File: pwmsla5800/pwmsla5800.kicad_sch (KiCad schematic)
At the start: 26 parts, among them Q1 BC547, Q2 BC547, U1 LM324

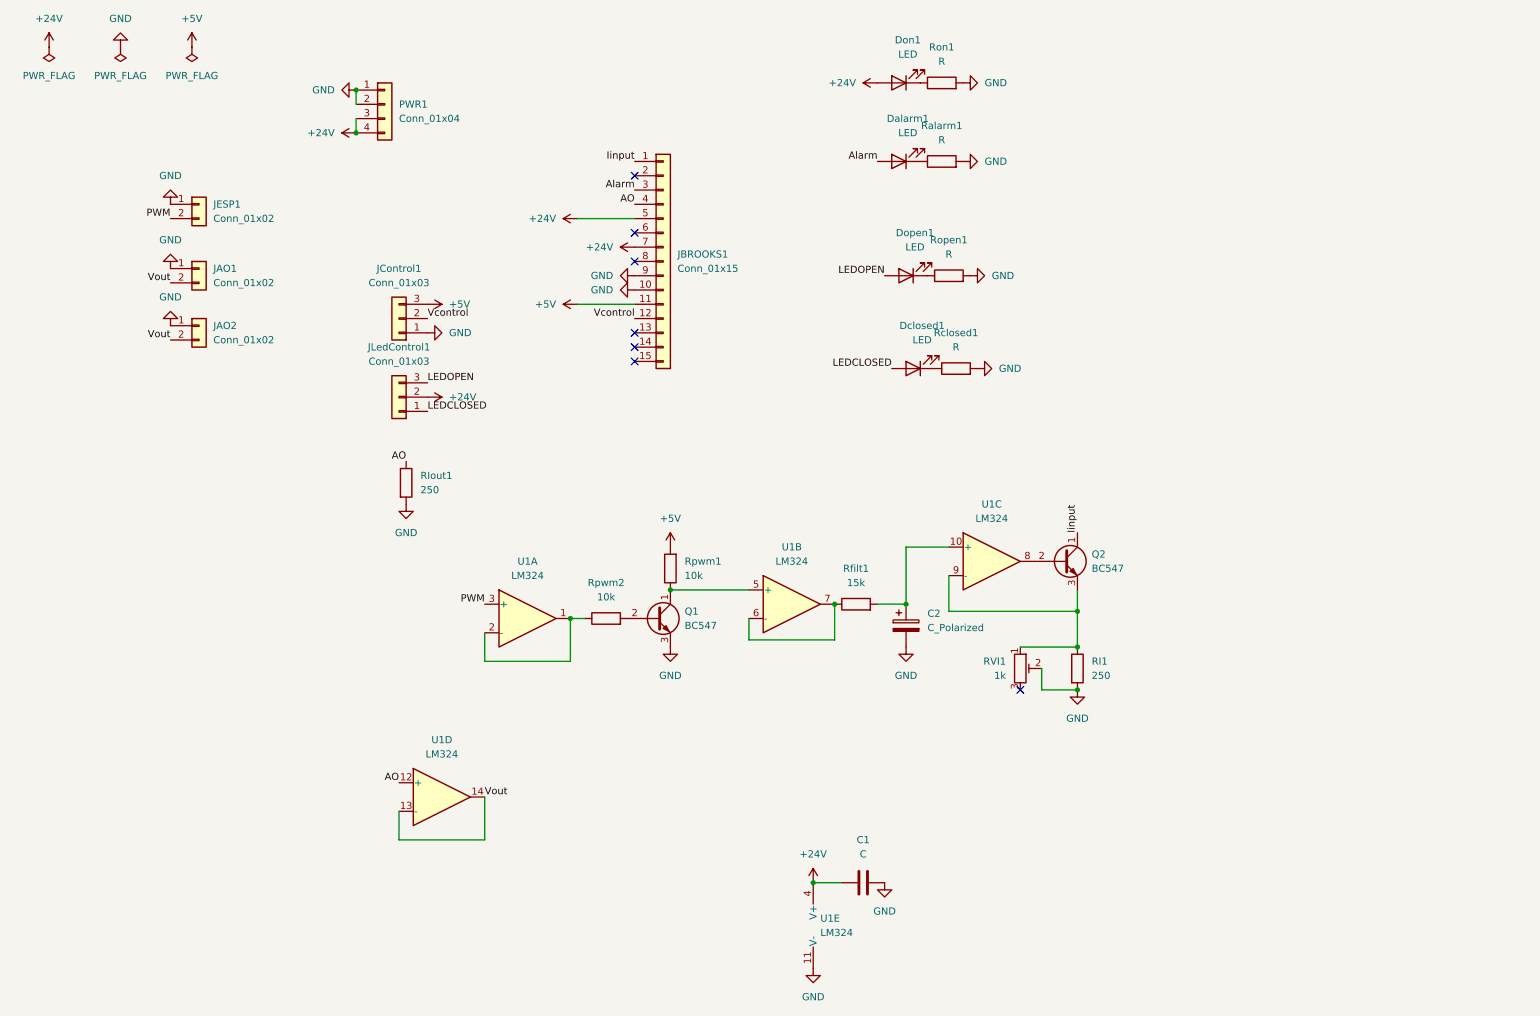
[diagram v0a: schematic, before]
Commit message: New concept. Generating the 4-20mA current is done on an outside module
Until I figure out how generate the current well, I think it is better just use a Chinese board.

When generating the PWM, to obtain a stable voltage I am using a TL431 circuit.
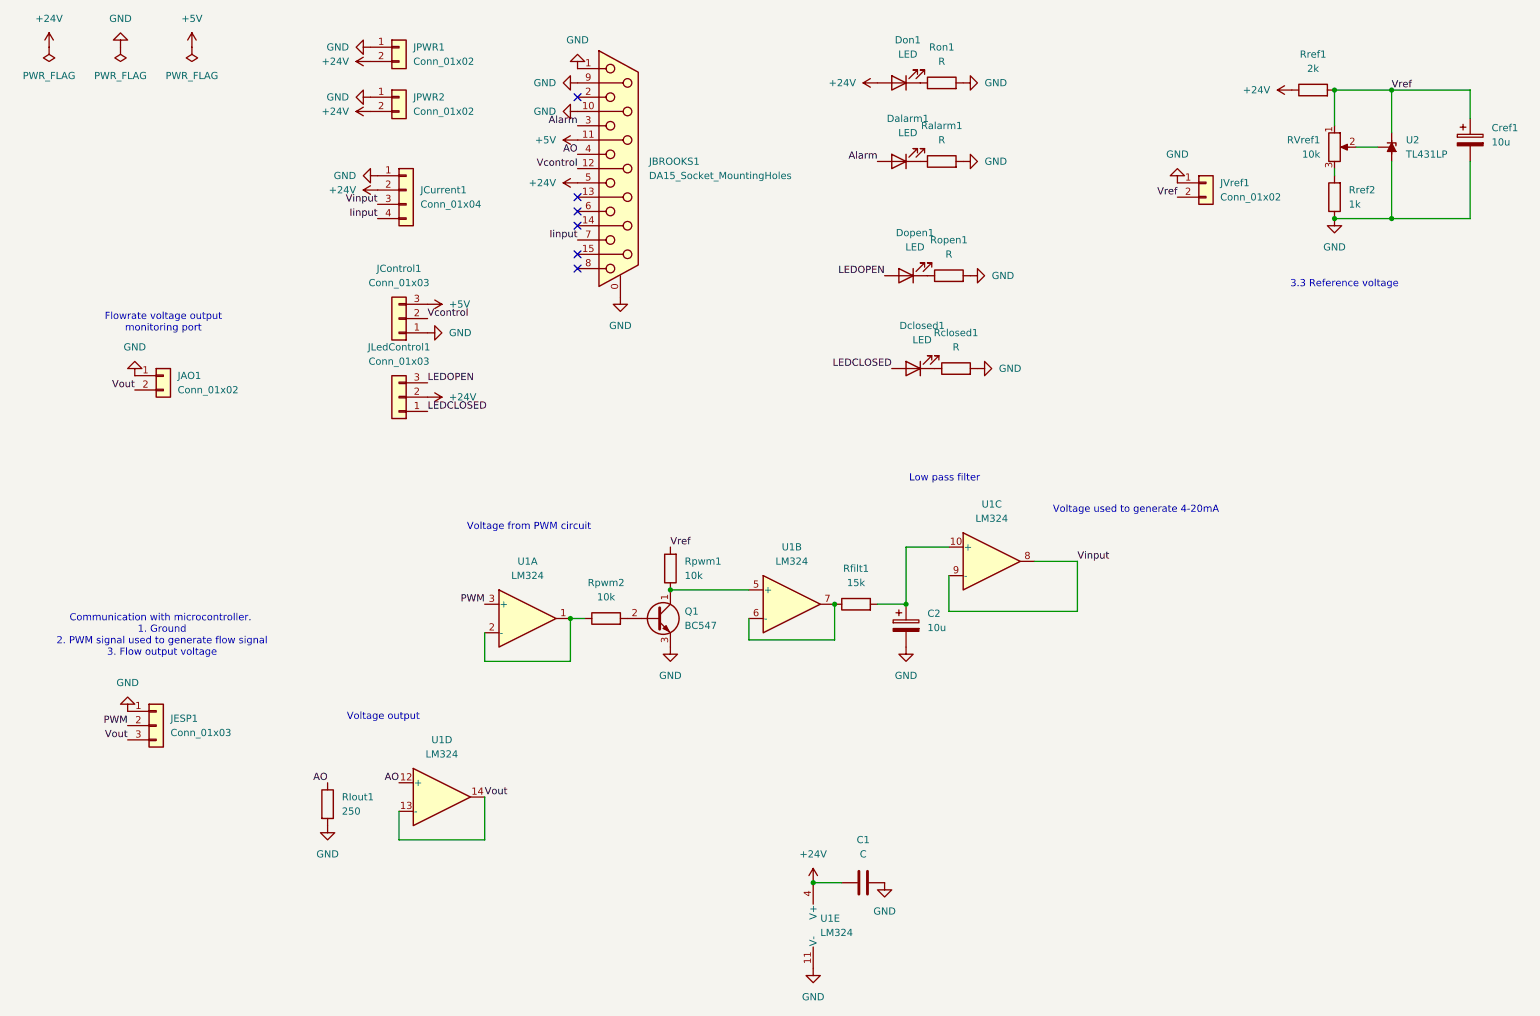
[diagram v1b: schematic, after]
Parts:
- removed JAO2, JESP1: Conn_01x02, Connector_PinHeader_2.54mm:PinHeader_1x02_P2.54mm_Vertical, symbol Connector_Generic:Conn_01x02
- removed JBROOKS1: Conn_01x15, Connector_Dsub:DSUB-15_Socket_Horizontal_P2.77x2.84mm_EdgePinOffset4.94mm_Housed_MountingHolesOffset4.94mm, symbol Connector_Generic:Conn_01x15
- removed PWR1: Conn_01x04, TerminalBlock:TerminalBlock_bornier-4_P5.08mm, symbol Connector_Generic:Conn_01x04
- removed Q2: BC547, Package_TO_SOT_THT:TO-92_Inline_Wide, symbol Transistor_BJT:BC547
- removed RI1: 250, Resistor_THT:R_Axial_DIN0207_L6.3mm_D2.5mm_P10.16mm_Horizontal, symbol Device:R
- removed RVI1: 1k, Potentiometer_THT:Potentiometer_Bourns_3296W_Vertical, symbol Device:R_Potentiometer_Trim
- added Cref1: 10u, Capacitor_THT:CP_Radial_D6.3mm_P2.50mm, symbol Device:C_Polarized
- added JBROOKS1: DA15_Socket_MountingHoles, Connector_Dsub:DSUB-15_Socket_Horizontal_P2.77x2.84mm_EdgePinOffset7.70mm_Housed_MountingHolesOffset9.12mm, symbol Connector:DA15_Socket_MountingHoles
- added JCurrent1: Conn_01x04, Connector_PinHeader_2.54mm:PinHeader_1x04_P2.54mm_Vertical, symbol Connector_Generic:Conn_01x04
- added JESP1: Conn_01x03, Connector_PinHeader_2.54mm:PinHeader_1x03_P2.54mm_Vertical, symbol Connector_Generic:Conn_01x03
- added JPWR1, JPWR2: Conn_01x02, Connector_Phoenix_MSTB:PhoenixContact_MSTBVA_2,5_2-G-5,08_1x02_P5.08mm_Vertical, symbol Connector_Generic:Conn_01x02
- added JVref1: Conn_01x02, Connector_PinHeader_2.54mm:PinHeader_1x02_P2.54mm_Vertical, symbol Connector_Generic:Conn_01x02
- added RVref1: 10k, Potentiometer_THT:Potentiometer_Bourns_3296W_Vertical, symbol Device:R_Potentiometer
- added Rref1: 2k, Resistor_THT:R_Axial_DIN0207_L6.3mm_D2.5mm_P10.16mm_Horizontal, symbol Device:R
- added Rref2: 1k, Resistor_THT:R_Axial_DIN0207_L6.3mm_D2.5mm_P10.16mm_Horizontal, symbol Device:R
- added U2: TL431LP, Package_TO_SOT_THT:TO-92_Inline_Wide, symbol Reference_Voltage:TL431LP
- C2: value C_Polarized -> 10u
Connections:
- net +24V: now also JBROOKS1.5, JCurrent1.2 (Pin_2), JPWR1.2 (Pin_2), JPWR2.2 (Pin_2), Rref1.1
- net +5V: now also JBROOKS1.11 (P111); no longer Rpwm1.2
- net AO: now also JBROOKS1.4
- net Alarm: now also JBROOKS1.3
- net GND: now also Cref1.2, JBROOKS1.0 (PAD), JBROOKS1.1, JBROOKS1.10 (P10), JBROOKS1.9 (P9), JCurrent1.1 (Pin_1), JESP1.1 (Pin_1), JPWR1.1 (Pin_1), JPWR2.1 (Pin_1), JVref1.1 (Pin_1), Rref2.1, U2.2 (A)
- net Iinput: now also JBROOKS1.7, JCurrent1.4 (Pin_4)
- net PWM: now also JESP1.2 (Pin_2)
- net Vcontrol: now also JBROOKS1.12 (P12)
- net Vout: now also JESP1.3 (Pin_3)
- net Vinput: now reaches U1.9 (-)
- net Vinput: now also U1.8, JCurrent1.3 (Pin_3)
- new net: RVref1.2, U2.1 (REF)
- new net: RVref1.3, Rref2.2
- new net Vref: Cref1.1, JVref1.2 (Pin_2), RVref1.1, Rpwm1.2, Rref1.2, U2.3 (K)
- no-connect marks 7 -> 6
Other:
- note added: "3.3 Reference voltage"
- note added: "Communication with microcontroller. 1. Ground 2. PWM signal used to generate flow signal 3. Flow output voltage"
- note added: "Flowrate voltage output monitoring port"
- note added: "Low pass filter"
- note added: "Voltage from PWM circuit"
- note added: "Voltage output"
- note added: "Voltage used to generate 4-20mA"
- moved on the sheet: JAO1, RIout1

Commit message: Corrected small bug in `pwm_mwtt.cpp` and updated R values in the board.
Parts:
- Ralarm1, Rclosed1, Ron1, Ropen1: value R -> 1.5k
- Rref2: value 1k -> 10k
